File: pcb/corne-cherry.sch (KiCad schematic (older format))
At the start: 142 parts, among them J1 MJ-4PP-9, J2 OLED, J3 MJ-4PP-9, J4 OLED, J5 Conn_01x01_Male, J6 Conn_01x01_Male, P1 Conn_01x03, P3 Conn_01x03, SW1 SW_PUSH, SW10 SW_PUSH, SW11 SW_PUSH, SW12 SW_PUSH, SW13 SW_PUSH, SW14 SW_PUSH, SW15 SW_PUSH, SW16 SW_PUSH, SW17 SW_PUSH, SW18 SW_PUSH, SW19 SW_PUSH, SW2 SW_PUSH, SW20 SW_PUSH, SW21 SW_PUSH, SW22 SW_PUSH, SW23 SW_PUSH, SW24 SW_PUSH, SW25 SW_PUSH, SW26 SW_PUSH, SW27 SW_PUSH, SW28 SW_PUSH, SW29 SW_PUSH, SW3 SW_PUSH, SW30 SW_PUSH, SW31 SW_PUSH, SW32 SW_PUSH, SW33 SW_PUSH, SW34 SW_PUSH, SW35 SW_PUSH, SW36 SW_PUSH, SW37 SW_PUSH, SW38 SW_PUSH, SW39 SW_PUSH, SW4 SW_PUSH, SW40 SW_PUSH, SW41 SW_PUSH, SW42 SW_PUSH, SW5 SW_PUSH, SW6 SW_PUSH, SW7 SW_PUSH, SW8 SW_PUSH, SW9 SW_PUSH, U1 ProMicro, U2 ProMicro

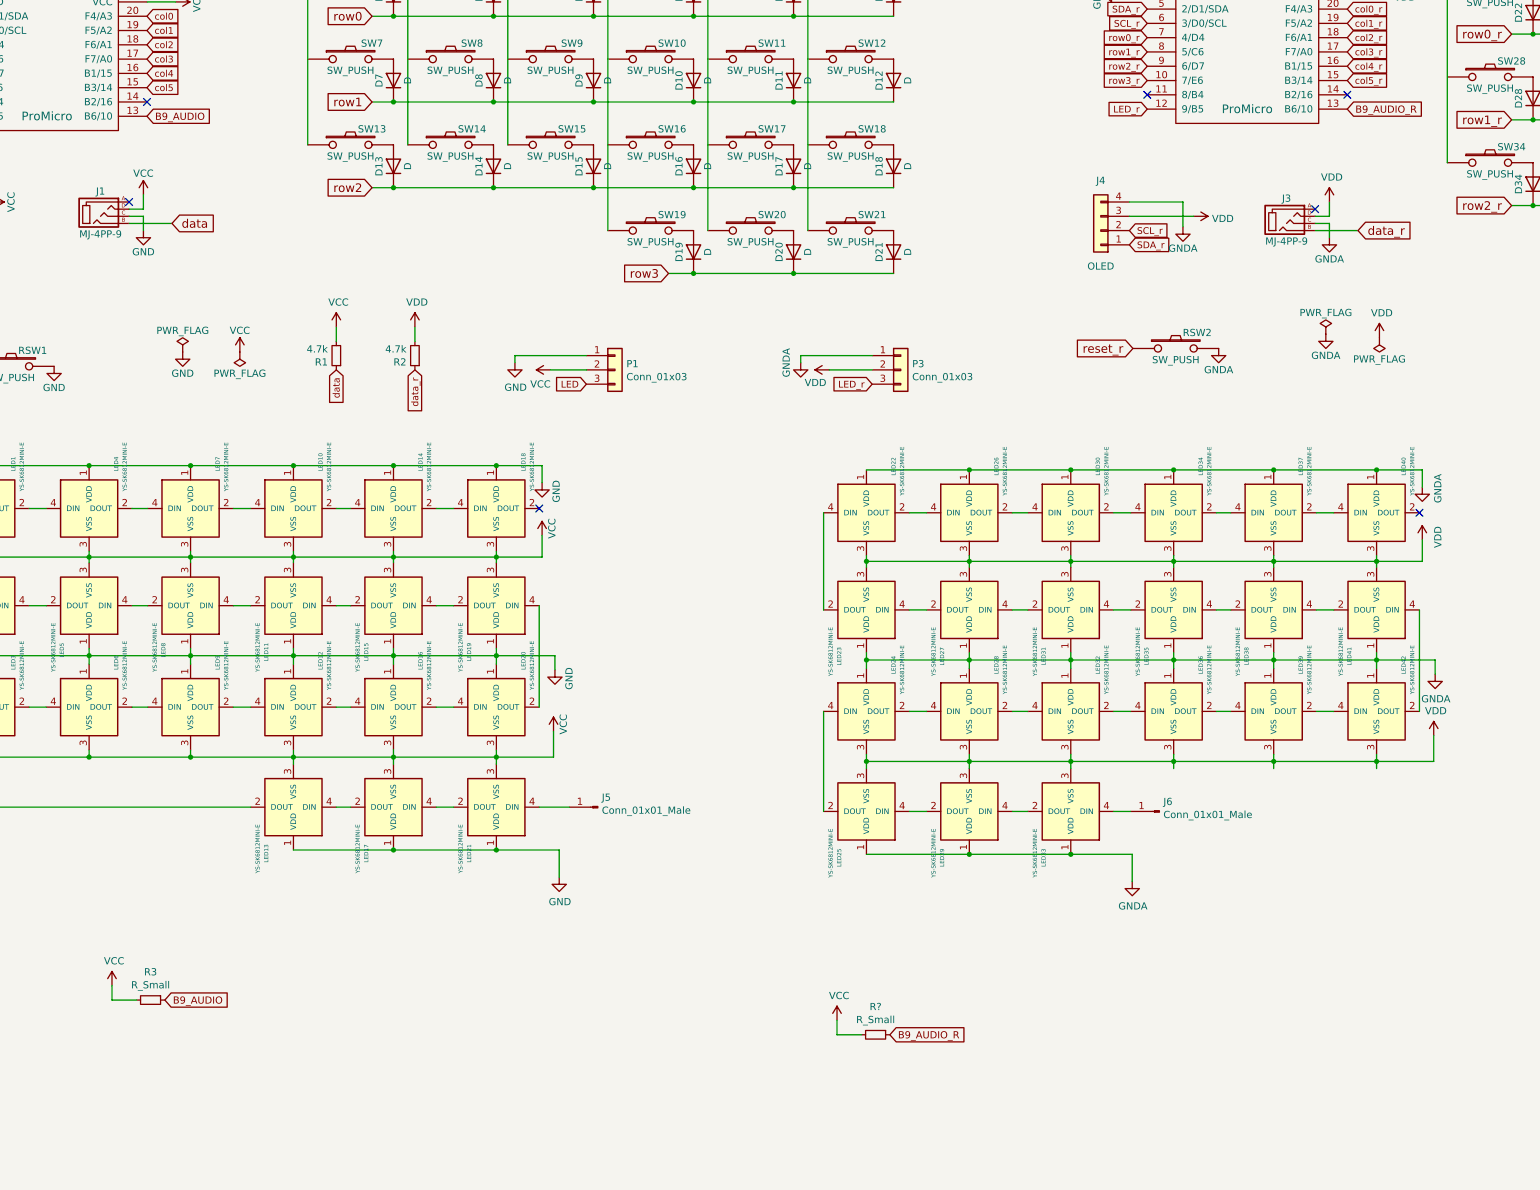
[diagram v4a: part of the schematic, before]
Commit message: Finish left half rgb with jumpers
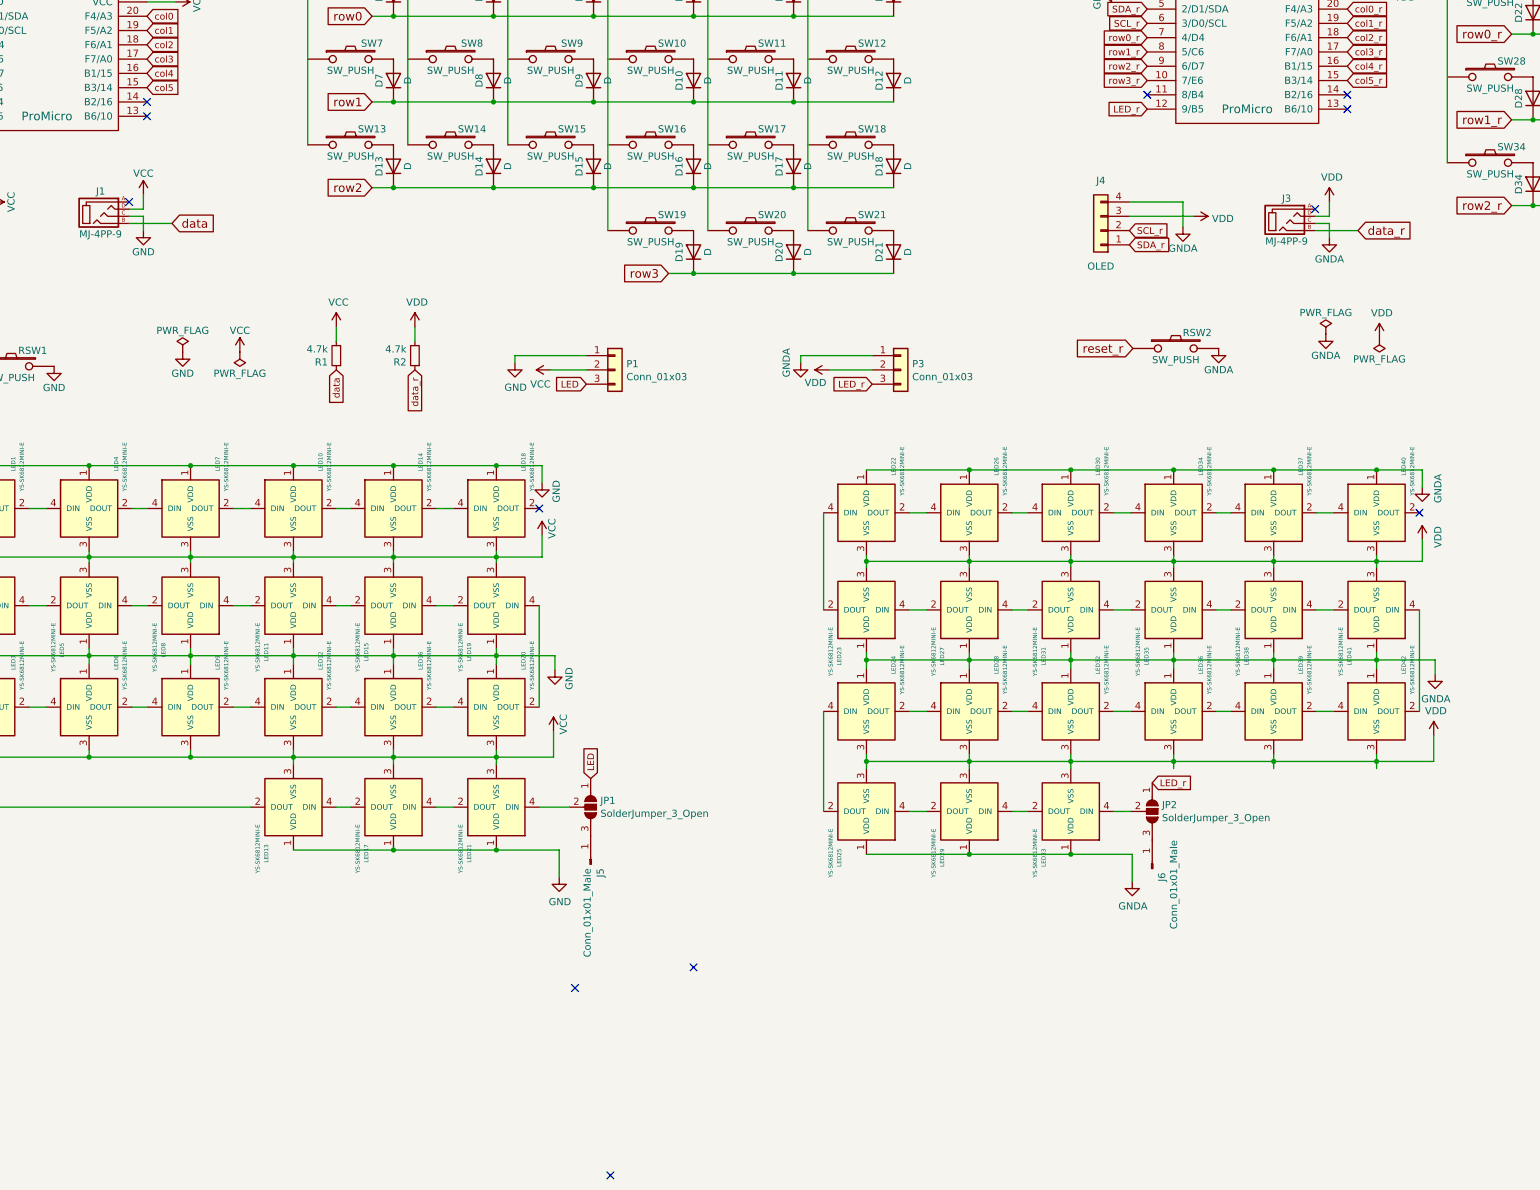
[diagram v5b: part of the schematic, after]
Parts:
- removed R3, R?: R_Small, symbol Device:R_Small
- added JP1, JP2: SolderJumper_3_Open, Jumper:SolderJumper-3_P1.3mm_Open_Pad1.0x1.5mm, symbol Jumper:SolderJumper_3_Open
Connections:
- net LED: now also JP1.1 (A)
- net LED_r: now also JP2.1 (A)
- net at LED33.4 (DIN): now also JP2.2 (C); no longer J6.1 (Pin_1)
- net at LED21.4 (DIN): now also JP1.2 (C); no longer J5.1 (Pin_1)
- net B9_AUDIO: no longer names the net of U1.13 (B6/10)
- net B9_AUDIO_R: no longer names the net of U2.13 (B6/10)
- new net: J6.1 (Pin_1), JP2.3 (B)
- new net: J5.1 (Pin_1), JP1.3 (B)
- no-connect marks 12 -> 17
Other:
- moved on the sheet: J5, J6
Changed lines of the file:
@@
 	6125 3375 6300 3375
-$Comp
-L kbd:ProMicro U2
-U 1 1 5C25F857
-P 10175 1675
-F 0 "U2" H 10175 2625 60  0000 C CNN
-F 1 "ProMicro" H 10175 1125 60  0000 C CNN
-F 2 "kbd:ProMicro_v3" H 10275 625 60  0001 C CNN
-F 3 "" H 10275 625 60  0000 C CNN
-	1    10175 1675
-	1    0    0    -1
-$EndComp
 $Comp
 L kbd:SW_PUSH SW23
@@
 	0    -1   -1   0
 $EndComp
-$Comp
-L Connector_Generic:Conn_01x03 P1
-U 1 1 5FEC8D74
-P 5750 4050
-F 0 "P1" H 5830 4092 50  0000 L CNN
-F 1 "Conn_01x03" H 5830 4001 50  0000 L CNN
-F 2 "Connector_PinSocket_2.54mm:PinSocket_1x03_P2.54mm_Vertical" H 5750 4050 50  0001 C CNN
-F 3 "~" H 5750 4050 50  0001 C CNN
-	1    5750 4050
-	1    0    0    -1
-$EndComp
 Wire Wire Line
 	5550 3950 5050 3950
@@
 	1    0    0    -1
 $EndComp
-Text GLabel 5550 4150 0    47   Input ~ 0
-LED
 Wire Wire Line
 	7550 3950 7050 3950
@@
 	1770 5700 1650 5700
 NoConn ~ 5220 5020
-$Comp
-L Connector:Conn_01x01_Male J5
-U 1 1 606C1E95
-P 5630 7110
-F 0 "J5" H 5602 7042 50  0000 R CNN
-F 1 "Conn_01x01_Male" H 5602 7133 50  0000 R CNN
-F 2 "Connector_PinHeader_2.54mm:PinHeader_1x01_P2.54mm_Vertical" H 5630 7110 50  0001 C CNN
-F 3 "~" H 5630 7110 50  0001 C CNN
-	1    5630 7110
-	-1   0    0    1
-$EndComp
-Wire Wire Line
-	5430 7110 5220 7110
 Wire Wire Line
 	1350 5360 2070 5360
@@
 L Connector:Conn_01x01_Male J6
 U 1 1 605E67F8
-P 9560 7140
-F 0 "J6" H 9532 7072 50  0000 R CNN
-F 1 "Conn_01x01_Male" H 9532 7163 50  0000 R CNN
-F 2 "Connector_PinHeader_2.54mm:PinHeader_1x01_P2.54mm_Vertical" H 9560 7140 50  0001 C CNN
-F 3 "~" H 9560 7140 50  0001 C CNN
-	1    9560 7140
-	-1   0    0    1
+P 9510 7540
+F 0 "J6" H 9482 7472 50  0000 R CNN
+F 1 "Conn_01x01_Male" H 9709 7389 50  0000 R CNN
+F 2 "Connector_PinHeader_2.54mm:PinHeader_1x01_P2.54mm_Vertical" H 9510 7540 50  0001 C CNN
+F 3 "~" H 9510 7540 50  0001 C CNN
+	1    9510 7540
+	0    -1   -1   0
 $EndComp
 Wire Wire Line
@@
 	1    0    0    -1
 $EndComp
-Wire Wire Line
-	2400 8460 2230 8460
-Text GLabel 2475 2275 2    50   Input ~ 0
-B9_AUDIO
+$Comp
+L Jumper:SolderJumper_3_Open JP1
+U 1 1 60654C8B
+P 5580 7110
+F 0 "JP1" V 5534 7178 50  0000 L CNN
+F 1 "SolderJumper_3_Open" V 5625 7178 50  0000 L CNN
+F 2 "Jumper:SolderJumper-3_P1.3mm_Open_Pad1.0x1.5mm" H 5580 7110 50  0001 C CNN
+F 3 "~" H 5580 7110 50  0001 C CNN
+	1    5580 7110
+	0    1    1    0
+$EndComp
+$Comp
+L Connector:Conn_01x01_Male J5
+U 1 1 606C1E95
+P 5580 7510
+F 0 "J5" H 5552 7442 50  0000 R CNN
+F 1 "Conn_01x01_Male" H 5552 7533 50  0000 R CNN
+F 2 "Connector_PinHeader_2.54mm:PinHeader_1x01_P2.54mm_Vertical" H 5580 7510 50  0001 C CNN
+F 3 "~" H 5580 7510 50  0001 C CNN
+	1    5580 7510
+	0    -1   -1   0
+$EndComp
+Text GLabel 5580 6910 1    47   Input ~ 0
+LED
+$Comp
+L Jumper:SolderJumper_3_Open JP2
+U 1 1 606B8CED
+P 9510 7140
+F 0 "JP2" V 9464 7208 50  0000 L CNN
+F 1 "SolderJumper_3_Open" V 9555 7208 50  0000 L CNN
+F 2 "Jumper:SolderJumper-3_P1.3mm_Open_Pad1.0x1.5mm" H 9510 7140 50  0001 C CNN
+F 3 "~" H 9510 7140 50  0001 C CNN
+	1    9510 7140
+	0    1    1    0
+$EndComp
+Wire Wire Line
+	5220 7110 5430 7110
+Text GLabel 9510 6940 2    47   Input ~ 0
+LED_r
 $Comp
 L kbd:ProMicro U1
@@
 	1    0    0    -1
 $EndComp
-$Comp
-L power:VCC #PWR0117
-U 1 1 608B3375
-P 2230 8360
-F 0 "#PWR0117" H 2230 8210 50  0001 C CNN
-F 1 "VCC" H 2245 8533 50  0000 C CNN
-F 2 "" H 2230 8360 50  0001 C CNN
-F 3 "" H 2230 8360 50  0001 C CNN
-	1    2230 8360
-	1    0    0    -1
-$EndComp
-Wire Wire Line
-	2230 8460 2230 8360
-Text GLabel 2600 8460 2    50   Input ~ 0
-B9_AUDIO
-$Comp
-L Device:R_Small R3
-U 1 1 60895581
-P 2500 8460
-F 0 "R3" V 2304 8460 50  0000 C CNN
-F 1 "R_Small" V 2395 8460 50  0000 C CNN
-F 2 "" H 2500 8460 50  0001 C CNN
-F 3 "~" H 2500 8460 50  0001 C CNN
-	1    2500 8460
-	0    1    1    0
-$EndComp
-Wire Wire Line
-	7474 8703 7304 8703
-$Comp
-L power:VCC #PWR?
-U 1 1 60A2BF96
-P 7304 8603
-F 0 "#PWR?" H 7304 8453 50  0001 C CNN
-F 1 "VCC" H 7319 8776 50  0000 C CNN
-F 2 "" H 7304 8603 50  0001 C CNN
-F 3 "" H 7304 8603 50  0001 C CNN
-	1    7304 8603
-	1    0    0    -1
-$EndComp
-Wire Wire Line
-	7304 8703 7304 8603
-Text GLabel 7674 8703 2    50   Input ~ 0
-B9_AUDIO_R
-$Comp
-L Device:R_Small R?
-U 1 1 60A2BFA2
-P 7574 8703
-F 0 "R?" V 7378 8703 50  0000 C CNN
-F 1 "R_Small" V 7469 8703 50  0000 C CNN
-F 2 "" H 7574 8703 50  0001 C CNN
-F 3 "~" H 7574 8703 50  0001 C CNN
-	1    7574 8703
-	0    1    1    0
-$EndComp
-Text GLabel 10875 2225 2    50   Input ~ 0
-B9_AUDIO_R
+NoConn ~ 2475 2275
+$Comp
+L kbd:ProMicro U2
+U 1 1 5C25F857
+P 10175 1675
+F 0 "U2" H 10175 2625 60  0000 C CNN
+F 1 "ProMicro" H 10175 1125 60  0000 C CNN
+F 2 "kbd:ProMicro_v3" H 10275 625 60  0001 C CNN
+F 3 "" H 10275 625 60  0000 C CNN
+	1    10175 1675
+	1    0    0    -1
+$EndComp
+NoConn ~ 10875 2225
+NoConn ~ 5718 9687
+NoConn ~ 5470 8376
+NoConn ~ 6300 8231
+Text GLabel 5550 4150 0    47   Input ~ 0
+LED
+$Comp
+L Connector_Generic:Conn_01x03 P1
+U 1 1 5FEC8D74
+P 5750 4050
+F 0 "P1" H 5830 4092 50  0000 L CNN
+F 1 "Conn_01x03" H 5830 4001 50  0000 L CNN
+F 2 "Connector_PinSocket_2.54mm:PinSocket_1x03_P2.54mm_Vertical" H 5750 4050 50  0001 C CNN
+F 3 "~" H 5750 4050 50  0001 C CNN
+	1    5750 4050
+	1    0    0    -1
+$EndComp
 $EndSCHEMATC
